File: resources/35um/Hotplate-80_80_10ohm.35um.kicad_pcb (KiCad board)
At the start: 2 copper layers, 80 x 80 mm, 7 parts, among them J1 Hotplate_Power_Connection, J2 Hotplate_Power_Connection

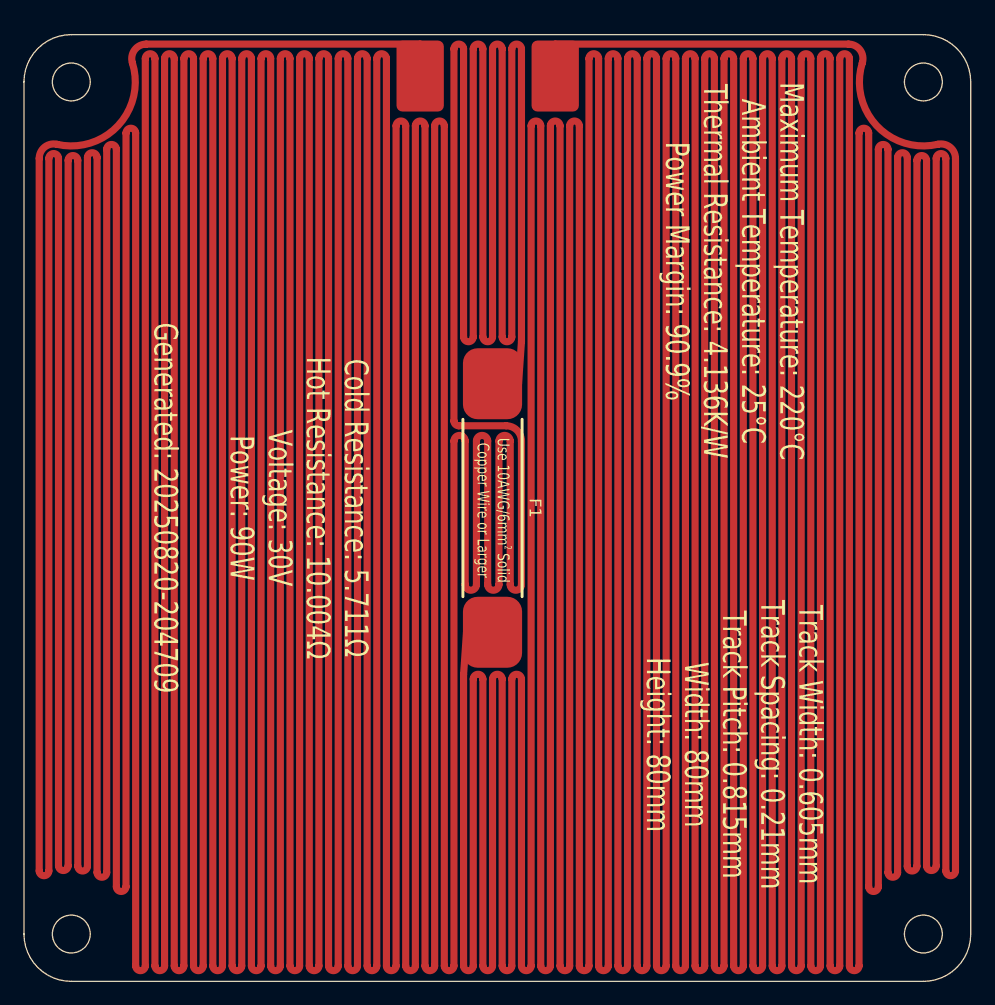
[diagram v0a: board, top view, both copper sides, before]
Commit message: Replaced obsolete 25mm thermal fuse footprint with new 35mm thermal fuse footprint.
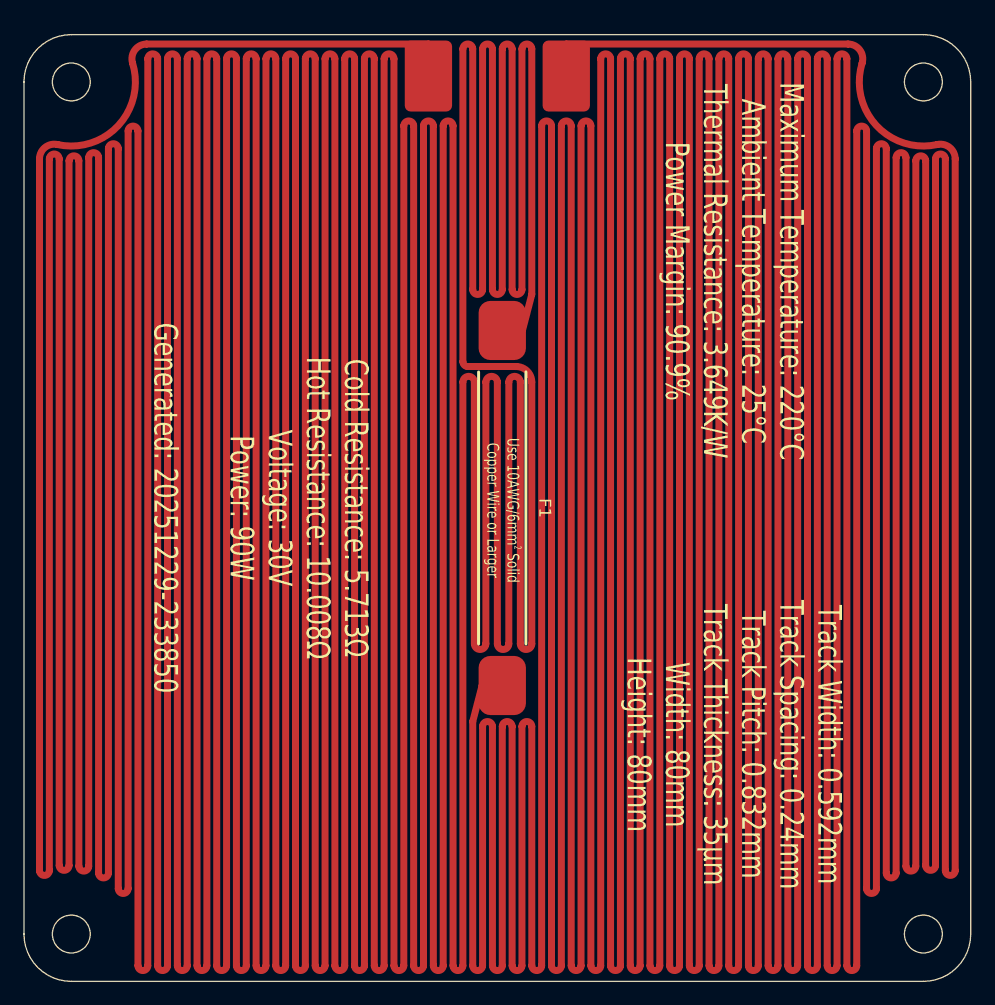
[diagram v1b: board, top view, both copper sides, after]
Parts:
- F1: footprint blg:Thermal Fuse, Front, 25mm -> blg:Thermal Fuse, SN100C, Front, 35mm
- moved J2 0.93 mm to (110.8, 68.5)
- moved F1 0.82 mm to (105.4, 105.0)
- moved J1 0.70 mm to (99.2, 68.5)
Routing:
- net Net-(J2-Pin_1): track 3526.6 -> 3341.7 mm
- net Net-(J1-Pin_1): track 3534.5 -> 3567.0 mm
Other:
- board text added: "Cold Resistance: 5.713Ω Hot Resistance: 10.008Ω Voltage: 30V Power: 90W Generated: 20251229-233850"
- board text added: "Maximum Temperature: 220°C Ambient Temperature: 25°C Thermal Resistance: 3.649K/W Power Margin: 90.9%"
- board text added: "Track Width: 0.592mm Track Spacing: 0.24mm Track Pitch: 0.832mm Track Thickness: 35µm Width: 80mm Height: 80mm"
- board text removed: "Cold Resistance: 5.711Ω Hot Resistance: 10.004Ω Voltage: 30V Power: 90W Generated: 20250820-204709"
- board text removed: "Maximum Temperature: 220°C Ambient Temperature: 25°C Thermal Resistance: 4.136K/W Power Margin: 90.9%"
- board text removed: "Track Width: 0.605mm Track Spacing: 0.21mm Track Pitch: 0.815mm Width: 80mm Height: 80mm"
